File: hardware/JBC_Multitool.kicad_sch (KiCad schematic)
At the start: 26 parts, among them J1 Screw_Terminal_01x02, U1 TPL7407LDR, U2 ESP32-WROOM-32, U3 TLV1117-33

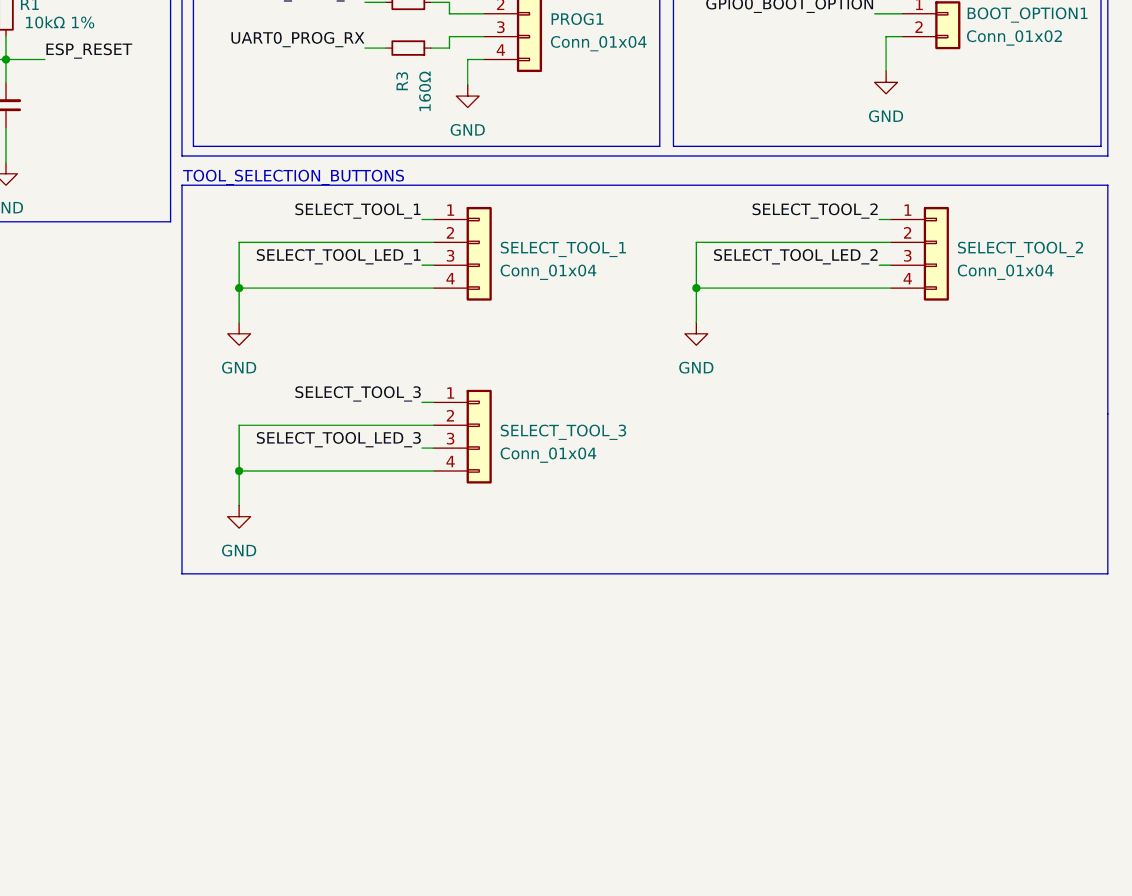
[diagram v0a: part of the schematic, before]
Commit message: corrected pin numbers on terminal footprint, changed switch-LED configuration
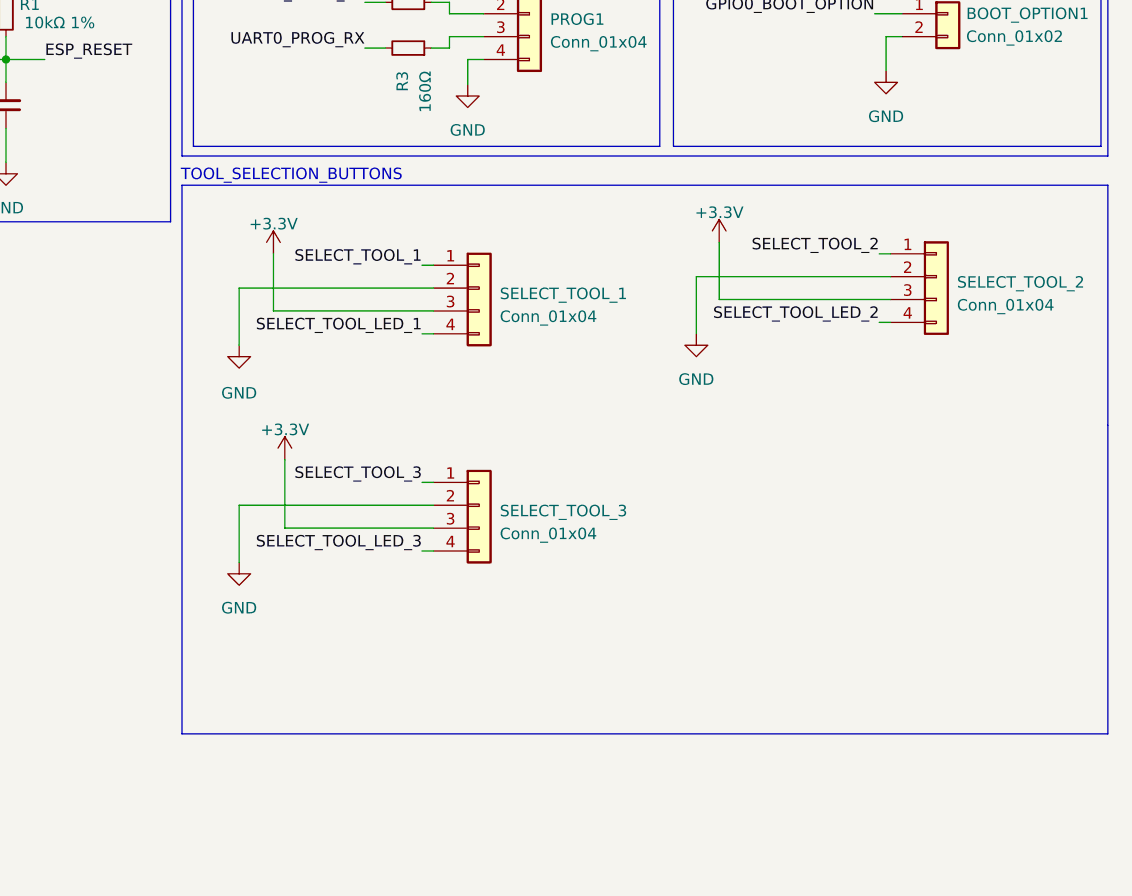
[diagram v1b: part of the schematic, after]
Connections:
- net +3.3V: now also SELECT_TOOL_1.3 (Pin_3), SELECT_TOOL_2.3 (Pin_3), SELECT_TOOL_3.3 (Pin_3)
- net GND: no longer SELECT_TOOL_1.4 (Pin_4), SELECT_TOOL_2.4 (Pin_4), SELECT_TOOL_3.4 (Pin_4)
- net SELECT_TOOL_LED_1: now also SELECT_TOOL_1.4 (Pin_4); no longer SELECT_TOOL_1.3 (Pin_3)
- net SELECT_TOOL_LED_2: now also SELECT_TOOL_2.4 (Pin_4); no longer SELECT_TOOL_2.3 (Pin_3)
- net SELECT_TOOL_LED_3: now also SELECT_TOOL_3.4 (Pin_4); no longer SELECT_TOOL_3.3 (Pin_3)
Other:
- moved on the sheet: SELECT_TOOL_1, SELECT_TOOL_2, SELECT_TOOL_3

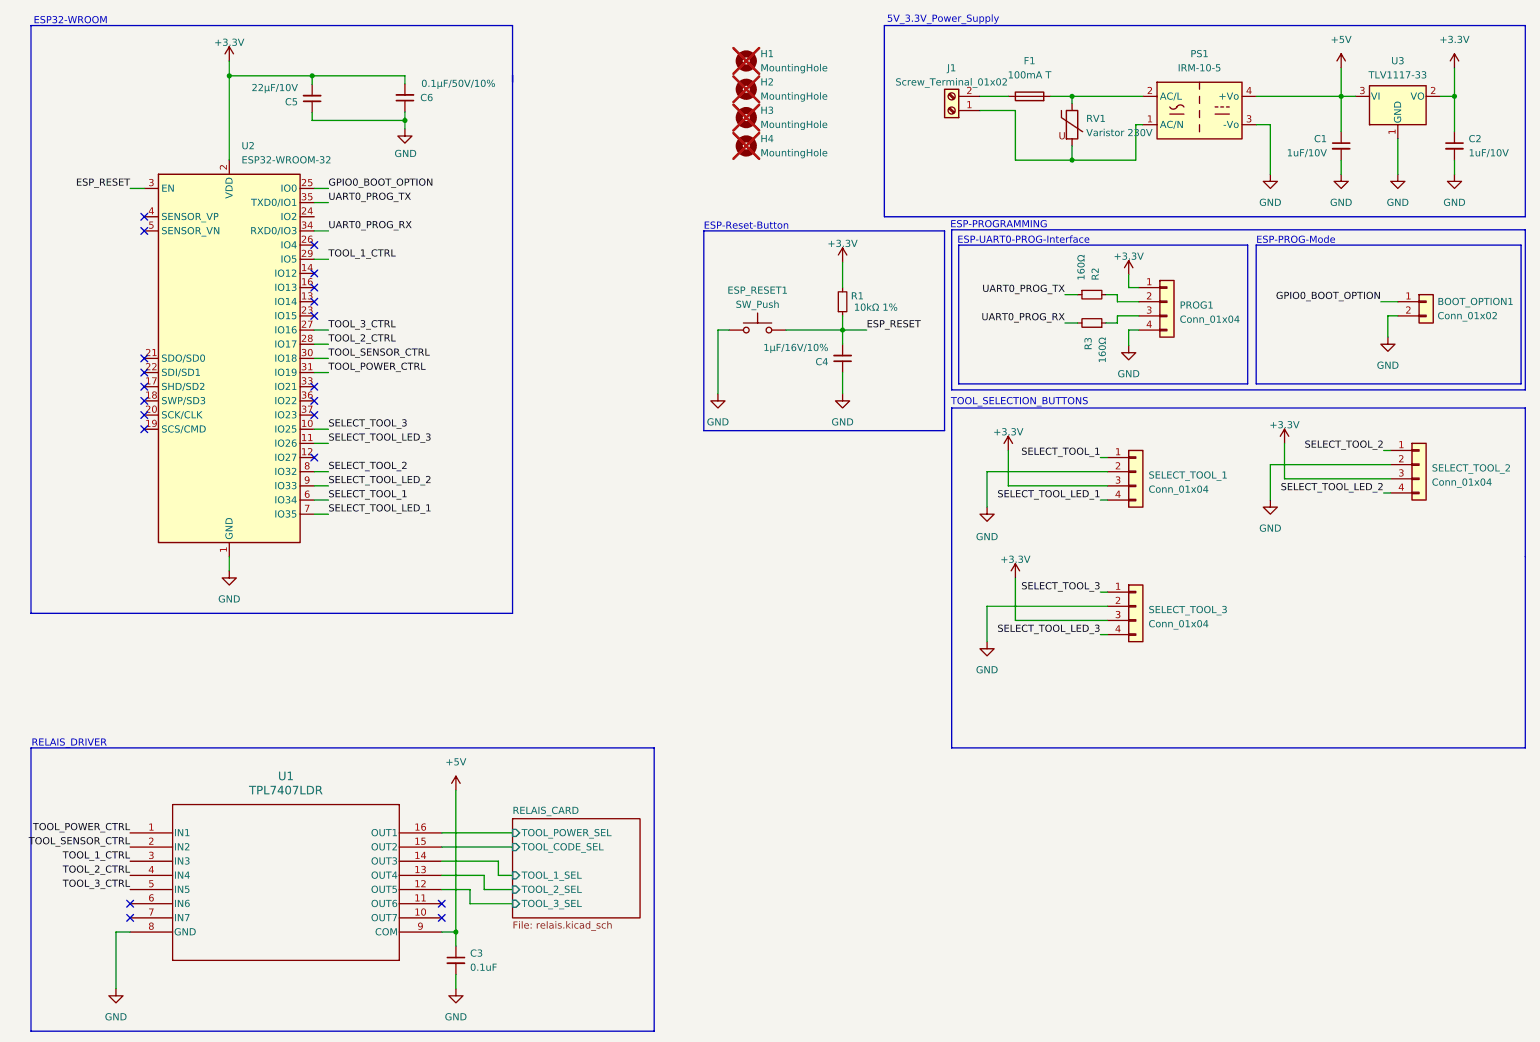
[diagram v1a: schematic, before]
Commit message: added 2.nd "old" jbc connector
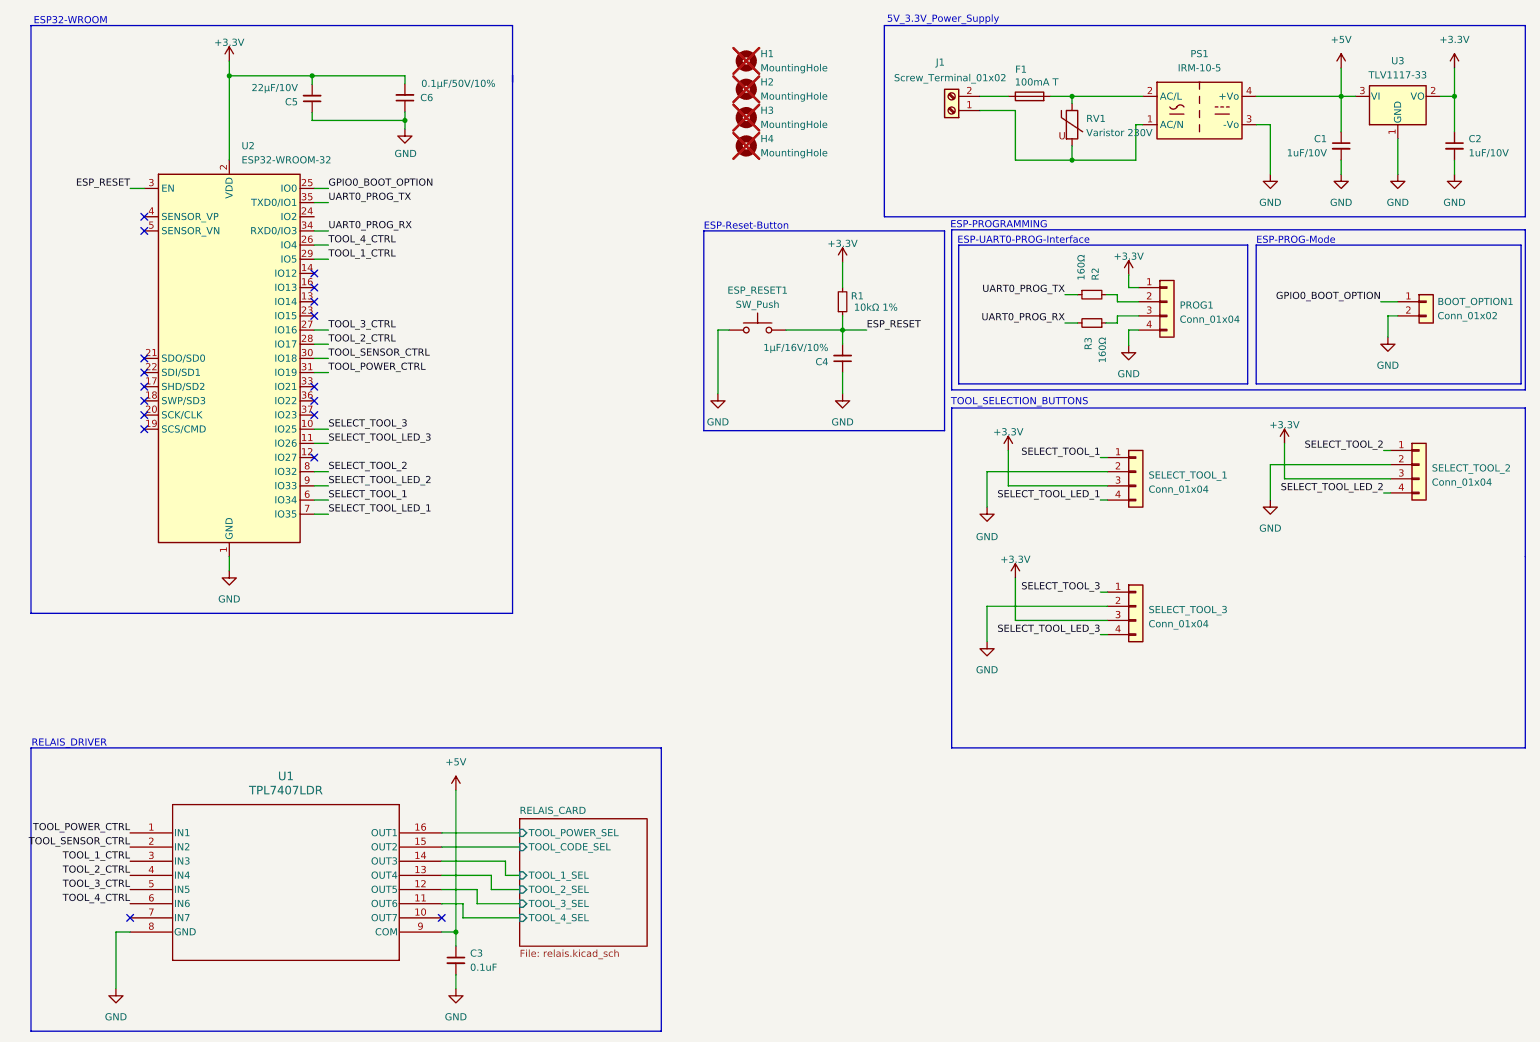
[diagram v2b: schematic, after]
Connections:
- net RELAIS_CARD/TOOL_4_SEL: now reaches U1.11 (OUT6)
- net TOOL_4_CTRL: now reaches U1.6 (IN6)
- net TOOL_4_CTRL: now also U2.26 (IO4)
- no-connect marks 21 -> 18
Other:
- sheet RELAIS_CARD ports: added TOOL_4_SEL; removed none
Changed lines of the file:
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@@
 	)
 	(no_connect
-		(at 64.77 54.61)
-	)
-	(no_connect
 		(at 64.77 64.77)
 	)
@@
 	)
 	(no_connect
-		(at 31.75 172.72)
-	)
-	(no_connect
 		(at 64.77 67.31)
 	)
@@
 	)
 	(no_connect
-		(at 87.63 172.72)
-	)
-	(no_connect
 		(at 31.75 175.26)
 	)
@@
 	(wire
 		(pts
-			(xy 87.63 165.1) (xy 97.79 165.1)
+			(xy 87.63 165.1) (xy 99.06 165.1)
 		)
 		(stroke
@@
 	(polyline
 		(pts
-			(xy 125.73 144.78) (xy 125.73 195.58)
+			(xy 127 144.78) (xy 127 195.58)
 		)
 		(stroke
@@
 	(wire
 		(pts
-			(xy 87.63 160.02) (xy 100.33 160.02)
+			(xy 87.63 160.02) (xy 101.6 160.02)
 		)
 		(stroke
@@
 	(wire
 		(pts
-			(xy 95.25 167.64) (xy 95.25 170.18)
+			(xy 96.52 167.64) (xy 96.52 170.18)
 		)
 		(stroke
@@
 	(wire
 		(pts
-			(xy 97.79 165.1) (xy 97.79 167.64)
+			(xy 99.06 165.1) (xy 99.06 167.64)
 		)
 		(stroke
@@
 	(wire
 		(pts
-			(xy 87.63 170.18) (xy 92.71 170.18)
+			(xy 87.63 170.18) (xy 93.98 170.18)
 		)
 		(stroke
@@
 	(wire
 		(pts
+			(xy 91.44 175.26) (xy 101.6 175.26)
+		)
+		(stroke
+			(width 0)
+			(type default)
+		)
+	)
+	(wire
+		(pts
 			(xy 205.74 92.71) (xy 207.01 92.71)
 		)
@@
 	(wire
 		(pts
+			(xy 87.63 172.72) (xy 91.44 172.72)
+		)
+		(stroke
+			(width 0)
+			(type default)
+		)
+	)
+	(wire
+		(pts
 			(xy 200.66 39.37) (xy 212.09 39.37)
 		)
@@
 	(wire
 		(pts
+			(xy 67.31 54.61) (xy 64.77 54.61)
+		)
+		(stroke
+			(width 0)
+			(type default)
+		)
+	)
+	(wire
+		(pts
 			(xy 259.08 35.56) (xy 259.08 41.91)
 		)
@@
 	(polyline
 		(pts
-			(xy 125.73 144.78) (xy 13.97 144.78)
+			(xy 127 144.78) (xy 13.97 144.78)
 		)
 		(stroke
@@
 	(wire
 		(pts
-			(xy 87.63 162.56) (xy 100.33 162.56)
+			(xy 87.63 162.56) (xy 101.6 162.56)
 		)
 		(stroke
@@
 	(polyline
 		(pts
-			(xy 13.97 195.58) (xy 125.73 195.58)
+			(xy 13.97 195.58) (xy 127 195.58)
 		)
 		(stroke
@@
 	(wire
 		(pts
-			(xy 92.71 172.72) (xy 100.33 172.72)
+			(xy 93.98 172.72) (xy 101.6 172.72)
 		)
 		(stroke
@@
 	(wire
 		(pts
-			(xy 92.71 170.18) (xy 92.71 172.72)
+			(xy 93.98 170.18) (xy 93.98 172.72)
 		)
 		(stroke
@@
 	(wire
 		(pts
-			(xy 95.25 170.18) (xy 100.33 170.18)
+			(xy 96.52 170.18) (xy 101.6 170.18)
 		)
 		(stroke
@@
 	(wire
 		(pts
-			(xy 97.79 167.64) (xy 100.33 167.64)
+			(xy 99.06 167.64) (xy 101.6 167.64)
 		)
 		(stroke
@@
 	(wire
 		(pts
+			(xy 91.44 172.72) (xy 91.44 175.26)
+		)
+		(stroke
+			(width 0)
+			(type default)
+		)
+	)
+	(wire
+		(pts
 			(xy 67.31 90.17) (xy 64.77 90.17)
 		)
@@
 	(wire
 		(pts
-			(xy 87.63 167.64) (xy 95.25 167.64)
+			(xy 87.63 167.64) (xy 96.52 167.64)
 		)
 		(stroke
@@
 		)
 	)
+	(label "TOOL_4_CTRL"
+		(at 31.75 172.72 180)
+		(fields_autoplaced yes)
+		(effects
+			(font
+				(size 1.27 1.27)
+			)
+			(justify right bottom)
+		)
+	)
 	(label "SELECT_TOOL_2"
 		(at 256.54 91.44 180)
@@
 		)
 	)
+	(label "TOOL_4_CTRL"
+		(at 67.31 54.61 0)
+		(fields_autoplaced yes)
+		(effects
+			(font
+				(size 1.27 1.27)
+			)
+			(justify left bottom)
+		)
+	)
 	(label "SELECT_TOOL_LED_2"
 		(at 256.54 99.06 180)
@@
 		(on_board yes)
 		(dnp no)
-		(fields_autoplaced yes)
 		(property "Reference" "F1"
-			(at 193.04 21.59 90)
+			(at 191.516 23.114 90)
 			(effects
 				(font
@@
 		)
 		(property "Value" "100mA T"
-			(at 193.04 24.13 90)
+			(at 194.31 25.4 90)
 			(effects
 				(font
@@
 		(on_board yes)
 		(dnp no)
-		(fields_autoplaced yes)
 		(property "Reference" "J1"
-			(at 179.07 22.86 0)
+			(at 177.038 21.844 0)
 			(effects
 				(font
@@
 		)
 		(property "Value" "Screw_Terminal_01x02"
-			(at 179.07 25.4 0)
+			(at 178.816 24.638 0)
 			(effects
 				(font
@@
 	)
 	(sheet
-		(at 100.33 157.48)
-		(size 22.86 17.78)
+		(at 101.6 157.48)
+		(size 22.86 22.86)
 		(fields_autoplaced yes)
 		(stroke
@@
 		)
 		(property "Sheetname" "RELAIS_CARD"
-			(at 100.33 156.7684 0)
+			(at 101.6 156.7684 0)
 			(effects
 				(font
@@
 		)
 		(property "Sheetfile" "relais.kicad_sch"
-			(at 100.33 175.8446 0)
+			(at 101.6 180.9246 0)
 			(effects
 				(font
@@
 		)
 		(pin "TOOL_POWER_SEL" input
-			(at 100.33 160.02 180)
+			(at 101.6 160.02 180)
 			(effects
 				(font
@@
 		)
 		(pin "TOOL_CODE_SEL" input
-			(at 100.33 162.56 180)
+			(at 101.6 162.56 180)
 			(effects
 				(font
@@
 		)
 		(pin "TOOL_1_SEL" input
-			(at 100.33 167.64 180)
+			(at 101.6 167.64 180)
 			(effects
 				(font
@@
 		)
 		(pin "TOOL_2_SEL" input
-			(at 100.33 170.18 180)
+			(at 101.6 170.18 180)
 			(effects
 				(font
@@
 		)
 		(pin "TOOL_3_SEL" input
-			(at 100.33 172.72 180)
+			(at 101.6 172.72 180)
+			(effects
+				(font
+					(size 1.27 1.27)
+				)
+				(justify left)
+			)
+		)
+		(pin "TOOL_4_SEL" input
+			(at 101.6 175.26 180)
 			(effects
 				(font

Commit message: added tool change switch 4
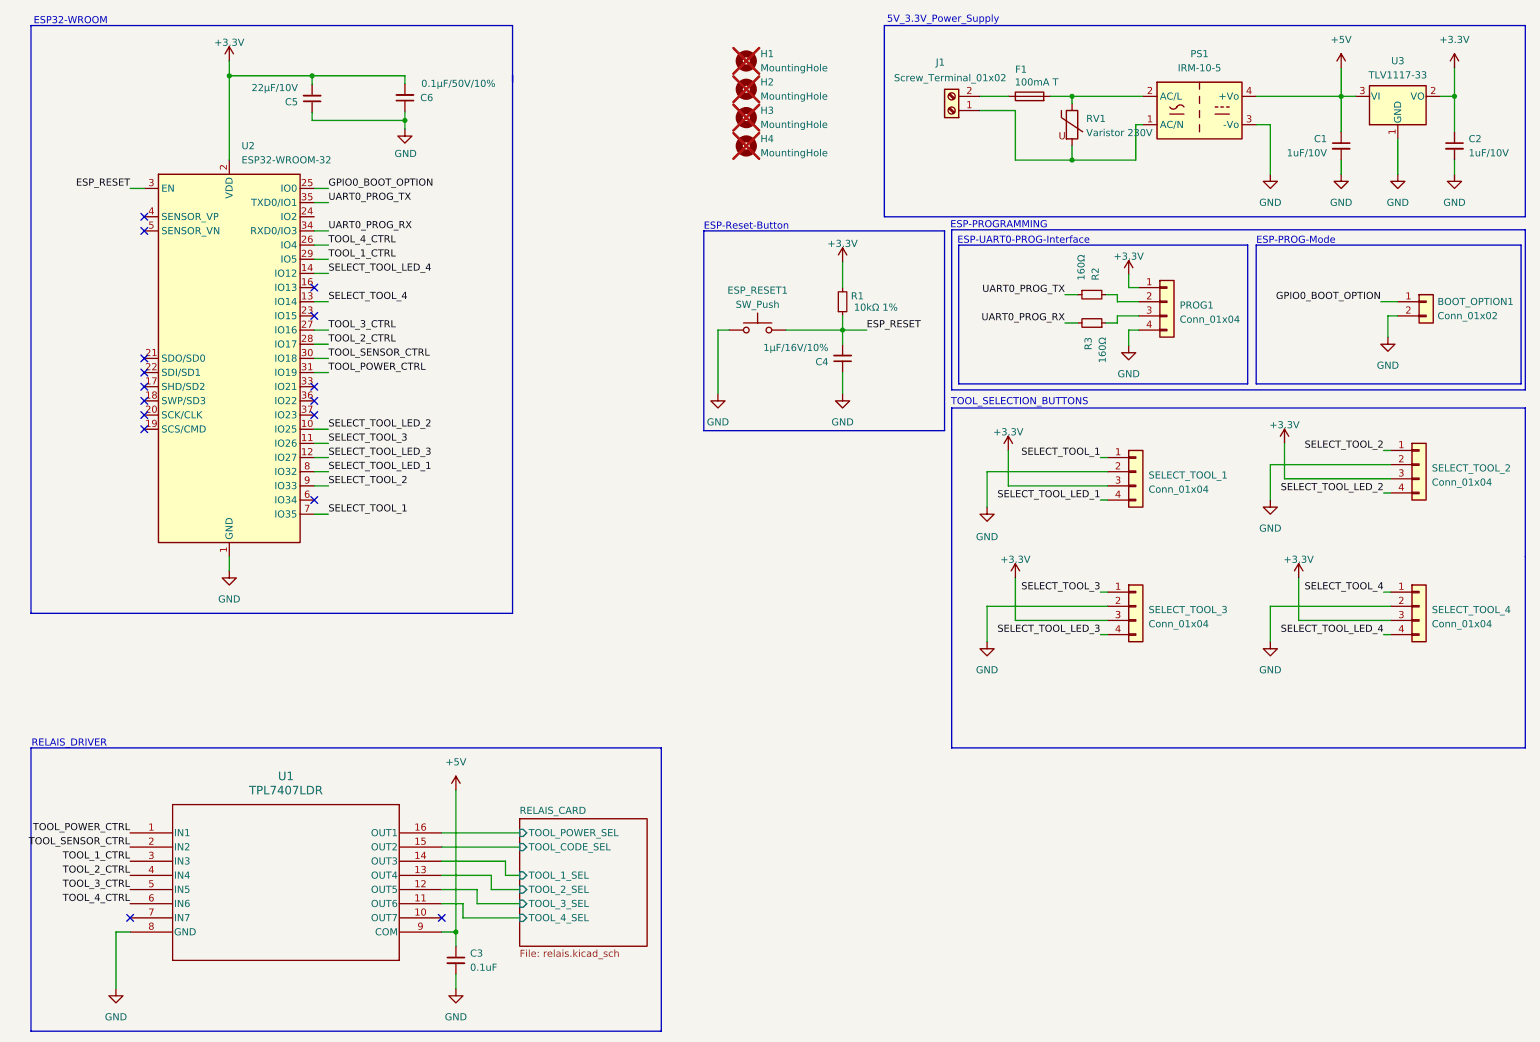
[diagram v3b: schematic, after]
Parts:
- added SELECT_TOOL_4: Conn_01x04, Connector_PinHeader_2.54mm:PinHeader_1x04_P2.54mm_Vertical, symbol Connector_Generic:Conn_01x04
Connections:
- net +3.3V: now also SELECT_TOOL_4.3 (Pin_3)
- net GND: now also SELECT_TOOL_4.2 (Pin_2)
- net SELECT_TOOL_1: now also U2.7 (IO35); no longer U2.6 (IO34)
- net SELECT_TOOL_2: now also U2.9 (IO33); no longer U2.8 (IO32)
- net SELECT_TOOL_3: now also U2.11 (IO26); no longer U2.10 (IO25)
- net SELECT_TOOL_LED_1: now also U2.8 (IO32); no longer U2.7 (IO35)
- net SELECT_TOOL_LED_2: now also U2.10 (IO25); no longer U2.9 (IO33)
- net SELECT_TOOL_LED_3: now also U2.12 (IO27); no longer U2.11 (IO26)
- net SELECT_TOOL_4: now reaches U2.13 (IO14)
- net SELECT_TOOL_4: now also SELECT_TOOL_4.1 (Pin_1)
- net SELECT_TOOL_LED_4: now reaches U2.14 (IO12)
- net SELECT_TOOL_LED_4: now also SELECT_TOOL_4.4 (Pin_4)
- no-connect marks 18 -> 16

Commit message: add gerber and bom
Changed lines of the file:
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@@
 	(polyline
 		(pts
-			(xy 179.07 144.78) (xy 179.07 83.82)
+			(xy 179.07 133.35) (xy 179.07 83.82)
 		)
 		(stroke
@@
 	(polyline
 		(pts
-			(xy 281.94 110.49) (xy 281.94 144.78)
+			(xy 281.94 110.49) (xy 281.94 133.35)
 		)
 		(stroke
@@
 	(polyline
 		(pts
-			(xy 281.94 144.78) (xy 179.07 144.78)
-		)
-		(stroke
+			(xy 281.94 133.35) (xy 179.07 133.35)
+		)
+		(stroke

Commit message: Add files via upload
PCB und Schaltplan überarbeitet.
GPIO5 & GPIO14 jetzt „not connected“, da diese GPIOs beim Boot auf HIGH gesetzt werden und die Relais und die LED anschalteten.
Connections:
- net SELECT_TOOL_1: now also U2.6 (IO34); no longer U2.7 (IO35)
- net SELECT_TOOL_2: now also U2.8 (IO32); no longer U2.9 (IO33)
- net SELECT_TOOL_3: now also U2.10 (IO25); no longer U2.11 (IO26)
- net SELECT_TOOL_4: now also U2.12 (IO27); no longer U2.13 (IO14)
- net SELECT_TOOL_LED_1: now also U2.7 (IO35); no longer U2.8 (IO32)
- net SELECT_TOOL_LED_2: now also U2.9 (IO33); no longer U2.10 (IO25)
- net SELECT_TOOL_LED_3: now also U2.11 (IO26); no longer U2.12 (IO27)
- net TOOL_1_CTRL: now also U2.30 (IO18); no longer U2.29 (IO5)
- net TOOL_POWER_CTRL: now also U2.33 (IO21); no longer U2.31 (IO19)
- net TOOL_SENSOR_CTRL: now also U2.31 (IO19); no longer U2.30 (IO18)
- no-connect marks 16 -> 17
